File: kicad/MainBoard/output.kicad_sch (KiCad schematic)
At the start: 125 parts, among them J11 CHAN1, J12 CHAN2, J13 Conn_01x02, J14 CHAN3, J15 CHAN4, Q10 AO3400A, Q11 AO3400A, Q12 IRF9Z24NPBF, Q13 AO3400A, Q18 AO3401A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

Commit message: Pcb v2.6 (#167)
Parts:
- added R156, R157: 10k, Resistor_SMD:R_0603_1608Metric_Pad0.98x0.95mm_HandSolder, symbol Device:R_Small
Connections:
- net ADC0: now also R157.1; no longer U9.31 (GPIO26_ADC0)
- net ADC1: now also R156.1; no longer U9.32 (GPIO27_ADC1)
- new net: R157.2, U9.31 (GPIO26_ADC0)
- new net: R156.2, U9.32 (GPIO27_ADC1)
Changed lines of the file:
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@@
   (title_block
     (title "ZC95 MKII")
-    (rev "2.5")
+    (rev "2.6")
     (company "CrashOverride85")
   )
@@
     (stroke (width 0) (type default) (color 0 0 0 0))
   )
+  (wire (pts (xy 67.31 226.441) (xy 67.31 226.695))
+    (stroke (width 0) (type default) (color 0 0 0 0))
+  )
   (wire (pts (xy 76.2 173.355) (xy 76.2 174.625))
     (stroke (width 0) (type default) (color 0 0 0 0))
@@
     (stroke (width 0) (type default) (color 0 0 0 0))
   )
+  (wire (pts (xy 68.326 226.441) (xy 67.31 226.441))
+    (stroke (width 0) (type default) (color 0 0 0 0))
+  )
   (wire (pts (xy 183.515 234.95) (xy 179.705 234.95))
     (stroke (width 0) (type default) (color 0 0 0 0))
@@
     (stroke (width 0) (type default) (color 0 0 0 0))
   )
+  (wire (pts (xy 67.31 239.395) (xy 68.326 239.395))
+    (stroke (width 0) (type default) (color 0 0 0 0))
+  )
   (wire (pts (xy 19.05 219.075) (xy 29.21 219.075))
     (stroke (width 0) (type default) (color 0 0 0 0))
@@
     )
   )
-  (global_label "ADC0" (shape input) (at 67.31 234.315 0) (fields_autoplaced)
+  (global_label "ADC0" (shape input) (at 68.326 239.395 0) (fields_autoplaced)
     (effects (font (size 1 1)) (justify left))
-    (property "Intersheet References" "${INTERSHEET_REFS}" (id 0) (at 73.0195 234.2525 0)
+    (property "Intersheet References" "${INTERSHEET_REFS}" (id 0) (at 74.0355 239.3325 0)
       (effects (font (size 1 1)) (justify left) hide)
     )
@@
     )
   )
-  (global_label "ADC1" (shape input) (at 67.31 231.775 0) (fields_autoplaced)
+  (global_label "ADC1" (shape input) (at 68.326 226.441 0) (fields_autoplaced)
     (effects (font (size 1 1)) (justify left))
-    (property "Intersheet References" "${INTERSHEET_REFS}" (id 0) (at 73.0195 231.7125 0)
+    (property "Intersheet References" "${INTERSHEET_REFS}" (id 0) (at 74.0355 226.3785 0)
       (effects (font (size 1 1)) (justify left) hide)
     )
@@
     (pin "1")
   )
+  (symbol (lib_id "Device:R_Small") (at 67.31 236.855 180) (unit 1)
+    (in_bom yes) (on_board yes)
+    (property "Reference" "R157" (id 0) (at 71.628 235.585 90))
+    (property "Value" "10k" (id 1) (at 69.342 236.093 90))
+    (property "Footprint" "Resistor_SMD:R_0603_1608Metric_Pad0.98x0.95mm_HandSolder" (id 2) (at 67.31 236.855 0)
+      (effects (font (size 1.27 1.27)) hide)
+    )
+    (property "Datasheet" "~" (id 3) (at 67.31 236.855 0)
+      (effects (font (size 1.27 1.27)) hide)
+    )
+    (property "LCSC" "C25804" (id 4) (at 67.31 236.855 90)
+      (effects (font (size 1.27 1.27)) hide)
+    )
+    (pin "1")
+    (pin "2")
+  )
   (symbol (lib_id "Amplifier_Operational:LM324") (at 27.94 88.265 270) (unit 5)
     (in_bom yes) (on_board yes)
@@
     (pin "1")
   )
+  (symbol (lib_id "Device:R_Small") (at 67.31 229.235 0) (unit 1)
+    (in_bom yes) (on_board yes)
+    (property "Reference" "R156" (id 0) (at 71.628 230.124 90))
+    (property "Value" "10k" (id 1) (at 69.215 229.362 90))
+    (property "Footprint" "Resistor_SMD:R_0603_1608Metric_Pad0.98x0.95mm_HandSolder" (id 2) (at 67.31 229.235 0)
+      (effects (font (size 1.27 1.27)) hide)
+    )
+    (property "Datasheet" "~" (id 3) (at 67.31 229.235 0)
+      (effects (font (size 1.27 1.27)) hide)
+    )
+    (property "LCSC" "C25804" (id 4) (at 67.31 229.235 90)
+      (effects (font (size 1.27 1.27)) hide)
+    )
+    (pin "1")
+    (pin "2")
+  )
   (symbol (lib_id "power:GND") (at 141.605 215.9 0) (unit 1)

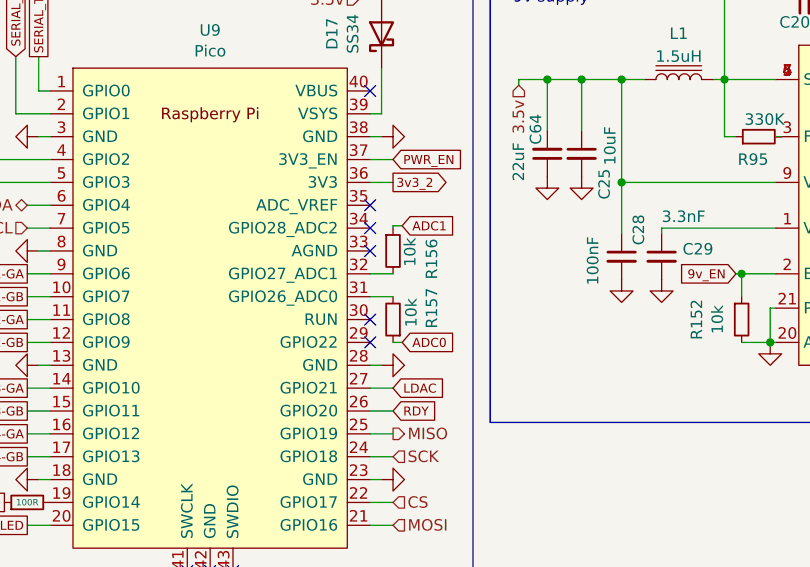
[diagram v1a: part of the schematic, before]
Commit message: update R156 and R157 to be 100R not 10K
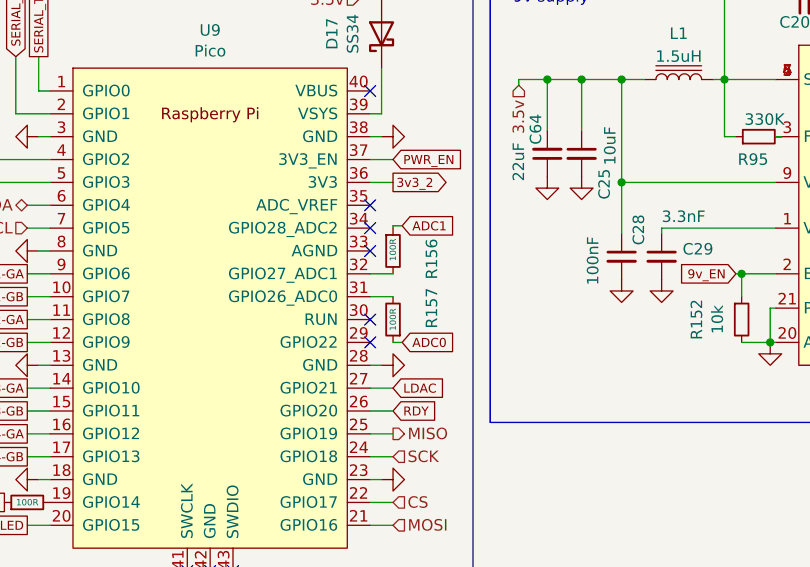
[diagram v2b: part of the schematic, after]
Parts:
- R156, R157: value 10k -> 100R; LCSC C25804 -> C22775
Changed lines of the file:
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@@
     (in_bom yes) (on_board yes)
     (property "Reference" "R157" (id 0) (at 71.628 235.585 90))
-    (property "Value" "10k" (id 1) (at 69.342 236.093 90))
+    (property "Value" "100R" (id 1) (at 67.31 236.855 90)
+      (effects (font (size 0.7 0.7)))
+    )
     (property "Footprint" "Resistor_SMD:R_0603_1608Metric_Pad0.98x0.95mm_HandSolder" (id 2) (at 67.31 236.855 0)
       (effects (font (size 1.27 1.27)) hide)
@@
       (effects (font (size 1.27 1.27)) hide)
     )
-    (property "LCSC" "C25804" (id 4) (at 67.31 236.855 90)
+    (property "LCSC" "C22775" (id 4) (at 67.31 236.855 90)
       (effects (font (size 1.27 1.27)) hide)
     )
@@
     (in_bom yes) (on_board yes)
     (property "Reference" "R156" (id 0) (at 71.628 230.124 90))
-    (property "Value" "10k" (id 1) (at 69.215 229.362 90))
+    (property "Value" "100R" (id 1) (at 67.31 229.108 90)
+      (effects (font (size 0.7 0.7)))
+    )
     (property "Footprint" "Resistor_SMD:R_0603_1608Metric_Pad0.98x0.95mm_HandSolder" (id 2) (at 67.31 229.235 0)
       (effects (font (size 1.27 1.27)) hide)
@@
       (effects (font (size 1.27 1.27)) hide)
     )
-    (property "LCSC" "C25804" (id 4) (at 67.31 229.235 90)
-      (effects (font (size 1.27 1.27)) hide)
-    )
+    (property "LCSC" "C22775" (id 4) (at 67.31 229.235 90)
+      (effects (font (size 1.27 1.27)) hide)
+    )
